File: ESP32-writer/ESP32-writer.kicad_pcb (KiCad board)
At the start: 2 copper layers, 27.2 x 30.6 mm, 17 parts, among them J1 USB2.0_C, J2 UART-OUTPUT, J3 USB2.0_C, Q1 2N7002, Q2 2N7002, U1 CH340C

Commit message: up
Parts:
- added U2: ESP-Prog-ProgramCOM-SEND, $74th:BoxPinHeader_2x03_P1.27mm_Vertical, F.Cu at (93.9, 68.6)
- moved C3 11.9 mm to (80.3, 64.4), turned to 180 degrees
- moved Q2 3.51 mm to (86.2, 86.8)
- moved Q1 3.50 mm to (86.2, 83.3)
- moved J2 2.60 mm to (94.0, 90.2)
- moved R3 2.33 mm to (79.8, 66.9)
- moved C2 1.44 mm to (79.9, 68.8)
- moved R1 1.10 mm to (80.0, 70.7)
- moved R2 0.77 mm to (80.0, 72.7)
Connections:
- Q1 pad 1: RTS -> DTR
- Q1 pad 2: DTS -> RTS
- Q2 pad 1: DTS -> RTS
- Q2 pad 2: RTS -> DTR
- U1 pad 13: DTS -> DTR
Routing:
- net DTS: track 23.1 -> 0.00 mm
- net DTR: track 0.00 -> 23.0 mm
- net RESET: track 10.4 -> 31.1 mm, vias 0 -> 2
- net +5V: track 89.9 -> 103.7 mm
- net BOOT: track 9.45 -> 22.2 mm
- net RXD: track 37.9 -> 48.4 mm
- net Net-(D1-Pad2): track 2.21 -> 7.86 mm, vias 0 -> 2
- net TXD: track 30.8 -> 35.3 mm
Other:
- board size 27.2 x 30.6 mm -> 31.2 x 30.5 mm
- board text added: "ESP32-Writer v2.0.0"
- board text added: "JLCJLCJLCJLC"
- board text removed: "ESP32-Writer v2.0"

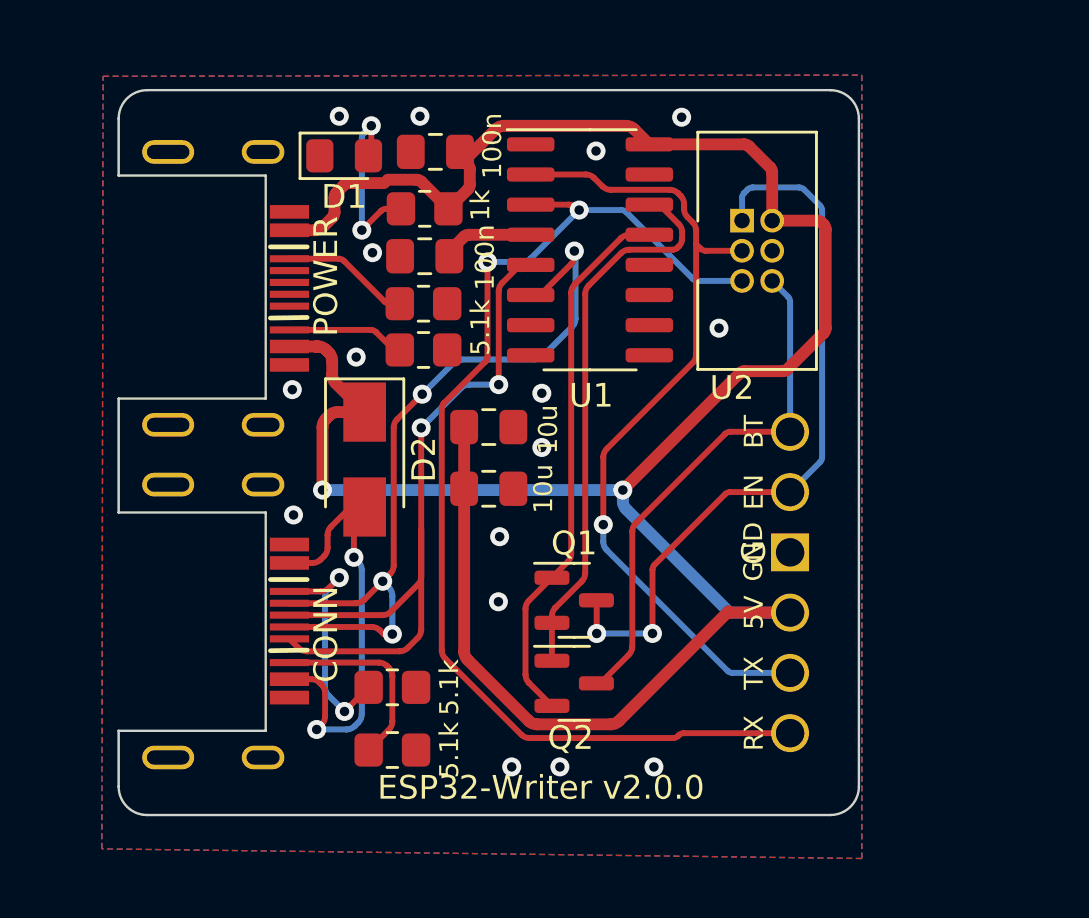
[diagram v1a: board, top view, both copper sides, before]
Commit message: ESP32-C3-WROOM-02
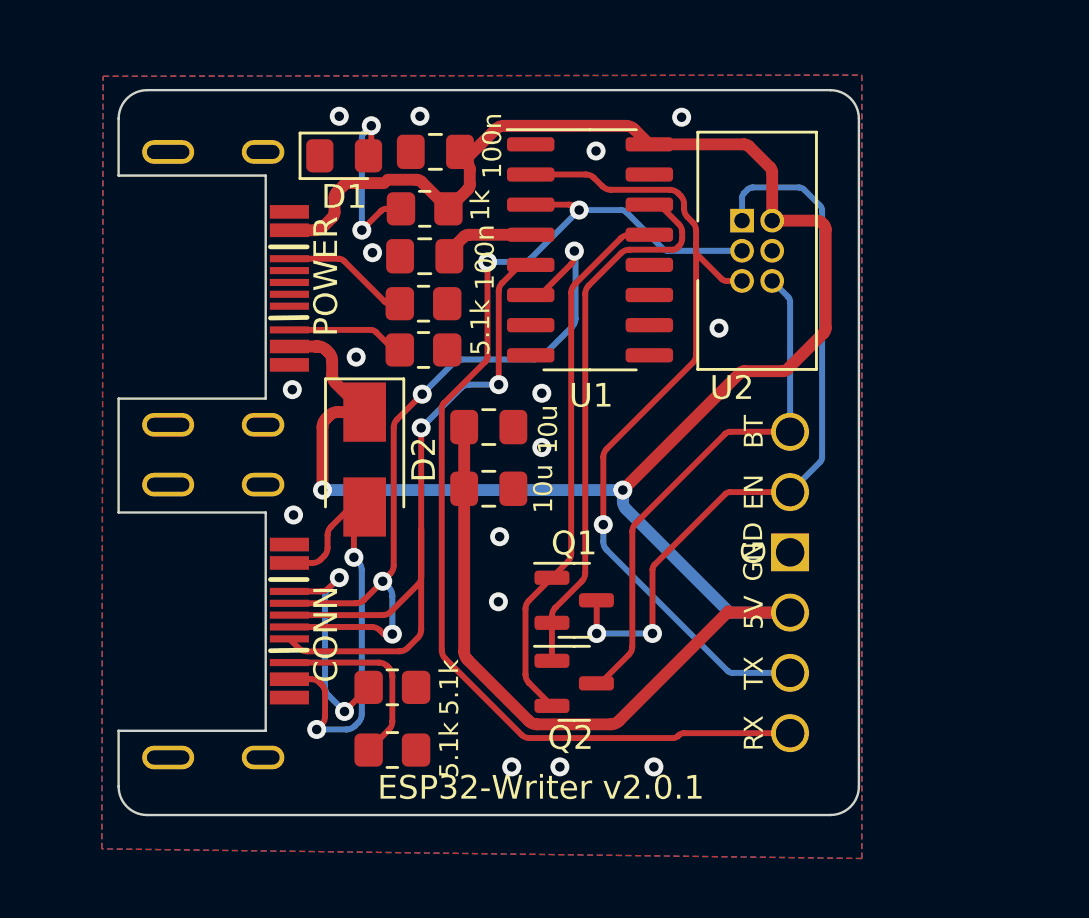
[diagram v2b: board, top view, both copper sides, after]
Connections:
- net +3V3 renamed +3.3V
- U2 pad 3: TXD -> RXD
- U2 pad 5: RXD -> TXD
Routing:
- net RXD: track 48.4 -> 47.9 mm
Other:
- board text added: "ESP32-Writer v2.0.1"
- board text removed: "ESP32-Writer v2.0.0"

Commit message: up
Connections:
- C2 pad 1: +3.3V -> Net-(SW1A-A)
- J1 pad 1: +5V -> Net-(J1-VBUS)
- J3 pad 1: Net-(D2-A) -> Net-(J3-VBUS)
- U1 pad 4: +3.3V -> Net-(SW1A-B)
- U1 pad 7: unconnected-(U1-NC) -> Net-(U1-XI)
- U1 pad 8: unconnected-(U1-OUT) -> Net-(U1-XO)
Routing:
- net Net-(J3-VBUS): track 0.00 -> 19.2 mm, vias 0 -> 2
- net Net-(D2-A): track 19.2 -> 0.00 mm, vias 2 -> 0
- net Net-(SW1A-A): track 0.00 -> 3.90 mm
- net +3.3V: track 3.90 -> 0.00 mm

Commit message: update esp32-writer
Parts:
- removed C2: 100n, $74th:Capacitor_0805_2012
- added C5: 100n, $74th:Capacitor_0805_2012, F.Cu at (82.9, 72.0)
- added C6: 22p, $74th:Capacitor_0805_2012, F.Cu at (91.6, 87.7)
- added C7: 22p, $74th:Capacitor_0805_2012, F.Cu at (83.7, 87.9)
- added C8: 1u, $74th:Capacitor_0805_2012, F.Cu at (91.8, 73.0)
- added F1: Polyfuse, $74th:ResettableFuse_KT6-1100SMDI, F.Cu at (79.1, 85.2)
- added F2: Polyfuse, $74th:ResettableFuse_KT6-1100SMDI, F.Cu at (79.1, 69.1)
- added J4: ESP-Prog-ProgramCOM-SEND, $74th:BoxPinHeader_2x03_P1.27mm_Vertical, F.Cu at (98.4, 67.6)
- added JP1: Jumper_3_Open, Jumper:SolderJumper-3_P1.3mm_Open_RoundedPad1.0x1.5mm_NumberLabels, F.Cu at (83.5, 77.7)
- added JP3: Jumper_2_Open, Jumper:SolderJumper-2_P1.3mm_Open_RoundedPad1.0x1.5mm, F.Cu at (83.4, 83.8)
- added Y1: 12M, $74th:Crystal_SMD_3225-4Pin_3.2x2.5mm_HandSoldering, F.Cu at (87.8, 87.8)
- C1: value 10u -> 1u
- C3: value 100n -> 1u
- C4: value 10u -> 100n
- D1: value LED -> D_Schottky; footprint $74th:LED_0805_2012Metric_Pad1.15x1.40mm_HandSolder -> $74th:D_SMA
- D2: value D_Schottky -> LED; footprint $74th:D_SMA -> $74th:LED_0805_2012Metric_Pad1.15x1.40mm_HandSolder
- J1: footprint $74th:USB-C-12-Pin-MidMount-ali-v4 -> $74th:USB-C-12-Pin-MidMount-ali-v5
- J2: value UART-OUTPUT -> USB2.0_C; footprint esp32-dev-board:UART -> $74th:USB-C-12-Pin-MidMount-ali-v5
- J3: value USB2.0_C -> UART-OUTPUT; footprint $74th:USB-C-12-Pin-MidMount-ali-v4 -> esp32-dev-board:UART
- R1, R2, R4: moved to B.Cu
- R3: value 1k -> 5.1k; moved to B.Cu
- R5: value 5.1k -> 200; moved to B.Cu
- U1: value CH340C -> AMS1117-3.3; footprint Package_SO:SOP-16_3.9x9.9mm_P1.27mm -> Package_TO_SOT_SMD:SOT-223-3_TabPin2
- U2: value ESP-Prog-ProgramCOM-SEND -> CH340G; footprint $74th:BoxPinHeader_2x03_P1.27mm_Vertical -> Package_SO:SOP-16_3.9x9.9mm_P1.27mm
- moved J3 29.8 mm to (102.1, 73.8)
- moved J2 27.7 mm to (67.0, 84.3), turned to -90 degrees
- moved R5 22.1 mm to (82.9, 67.8), turned to 90 degrees
- moved C4 15.6 mm to (96.7, 85.2), turned to 180 degrees
- moved C3 14.2 mm to (93.6, 69.5), turned to 90 degrees
- moved Q2 14.1 mm to (96.6, 77.3)
- moved D1 12.6 mm to (79.0, 76.9), turned to -90 degrees
- moved C1 12.1 mm to (83.0, 63.9), turned to 180 degrees
- moved U2 11.5 mm to (89.9, 79.4)
- moved D2 11.1 mm to (82.9, 67.8), turned to 90 degrees
- moved Q1 10.5 mm to (96.5, 81.3)
- moved R2 10.5 mm to (79.4, 83.1)
- moved J1 7.20 mm to (67.0, 70.1)
- moved R3 4.16 mm to (79.1, 71.0), turned to 0 degrees
- moved U1 2.54 mm to (88.9, 67.0), turned to -90 degrees
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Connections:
- C3 pad 1: +5V -> +3V3
- C4 pad 1: +5V -> RESET
- D1 pad 1: GND -> +5V
- D2 pad 1: +5V -> GND
- J2 pad 1: RXD -> Net-(J2-VBUS)
- J2 pad 2: TXD -> DM
- J2 pad 3: +5V -> DP
- J2 pad 5: RESET -> Net-(J2-CC1)
- J2 pad 6: BOOT -> Net-(J2-CC2)
- J3 pad 1: Net-(J3-VBUS) -> RXD
- J3 pad 2: DM -> TXD
- J3 pad 3: DP -> +5V
- J3 pad 4: GND -> +3V3
- J3 pad 5: Net-(J3-CC1) -> GND
- J3 pad 6: Net-(J3-CC2) -> RESET
- R2 pad 1: Net-(J1-CC2) -> Net-(J2-CC1)
- R3 pad 1: +5V -> Net-(J1-CC2)
- R3 pad 2: Net-(D1-A) -> GND
- R4 pad 1: Net-(J3-CC1) -> Net-(J2-CC2)
- R5 pad 1: Net-(J3-CC2) -> +5V
- R5 pad 2: GND -> Net-(D2-A)
- U1 pad 2: TXD -> +3V3
- U1 pad 3: RXD -> +5V
- U2 pad 1: RESET -> GND
- U2 pad 2: +5V -> TXD
- U2 pad 4: GND -> Net-(JP1-C)
- U2 pad 5: TXD -> DP
- U2 pad 6: BOOT -> DM
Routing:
- net +3V3: track 0.00 -> 54.2 mm, vias 0 -> 2
- net +5V: track 103.7 -> 74.1 mm, vias 2 -> 1
- net Net-(J3-VBUS): track 19.2 -> 0.00 mm, vias 2 -> 0
- net DTR: track 23.0 -> 5.54 mm
- net RXD: track 47.9 -> 30.6 mm, vias 2 -> 1
- net DM: track 33.1 -> 17.5 mm, vias 4 -> 3
- net Net-(JP3-B): track 0.00 -> 14.2 mm
- net RTS: track 23.4 -> 10.4 mm
- net Net-(J2-VBUS): track 0.00 -> 12.9 mm
- net DP: track 32.8 -> 20.1 mm
- net Net-(J1-VBUS): track 0.00 -> 12.5 mm
- net Net-(J3-CC1): track 9.94 -> 0.00 mm, vias 2 -> 0
- net GND: track 0.07 -> 9.50 mm, vias 16 -> 26
- net Net-(J3-CC2): track 8.15 -> 0.00 mm
- net TXD: track 35.6 -> 28.1 mm
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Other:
- board size 31.2 x 30.5 mm -> 36.4 x 30.7 mm
- board text added: "ESP32-Writer v2.1.0"
- board text added: "R232"
- board text removed: "ESP32-Writer v2.0.1"

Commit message: type-b
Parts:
- renumbered C5 to C2, C7 to C3, C8 to C4, C6 to C5, C3 to C6, C4 to C7, F2 to F1, F1 to F2, J4 to J3, J3 to J4, JP3 to JP2, Q2 to Q1, Q1 to Q2, R5 to R1, R4 to R3, R1 to R4, R3 to R5
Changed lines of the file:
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@@
     (property "ki_keywords" "cap capacitor")
     (attr smd)
-    (fp_text reference "C8" (at 2.3 0.2 90) (layer "F.SilkS")
+    (fp_text reference "C4" (at 2.3 0.2 90) (layer "F.SilkS")
         (effects (font (size 0.8 0.8) (thickness 0.12)))
     )
@@
     (property "ki_keywords" "cap capacitor")
     (attr smd)
-    (fp_text reference "C5" (at 0 1.45 90) (layer "F.SilkS")
+    (fp_text reference "C2" (at 0 1.45 90) (layer "F.SilkS")
         (effects (font (size 0.8 0.8) (thickness 0.12)))
     )
@@
     (property "ki_keywords" "cap capacitor")
     (attr smd)
-    (fp_text reference "C4" (at 2.3 0.1 90) (layer "F.SilkS")
+    (fp_text reference "C7" (at 2.3 0.1 90) (layer "F.SilkS")
         (effects (font (size 0.8 0.8) (thickness 0.12)))
     )
@@
     (property "ki_keywords" "N-Channel Switching MOSFET")
     (attr smd)
-    (fp_text reference "Q2" (at -2.2625 0.3 90) (layer "F.SilkS")
+    (fp_text reference "Q1" (at -2.2625 0.3 90) (layer "F.SilkS")
         (effects (font (size 1 1) (thickness 0.15)))
     )
@@
     (property "ki_keywords" "resettable fuse PTC PPTC polyfuse polyswitch")
     (attr smd)
-    (fp_text reference "F2" (at 0.1 0.1 90 unlocked) (layer "F.SilkS")
+    (fp_text reference "F1" (at 0.1 0.1 90 unlocked) (layer "F.SilkS")
         (effects (font (size 0.8 0.8) (thickness 0.12)))
     )
@@
     (property "ki_keywords" "resettable fuse PTC PPTC polyfuse polyswitch")
     (attr smd)
-    (fp_text reference "F1" (at 0.3 0.1 90 unlocked) (layer "F.SilkS")
+    (fp_text reference "F2" (at 0.3 0.1 90 unlocked) (layer "F.SilkS")
         (effects (font (size 0.8 0.8) (thickness 0.12)))
     )
@@
     (property "Sheetname" "")
     (attr through_hole)
-    (fp_text reference "J3" (at 7.62 -5.715 -90 unlocked) (layer "F.Fab")
+    (fp_text reference "J4" (at 7.62 -5.715 -90 unlocked) (layer "F.Fab")
         (effects (font (size 1 1) (thickness 0.15)))
     )
@@
     (property "ki_description" "Jumper, 2-pole, open")
     (property "ki_keywords" "Jumper SPST")
-    (fp_text reference "JP3" (at -0.1 2.3 90) (layer "F.SilkS")
+    (fp_text reference "JP2" (at -0.1 2.3 90) (layer "F.SilkS")
         (effects (font (size 1 1) (thickness 0.15)))
     )
@@
     (property "Sheetname" "")
     (attr through_hole)
-    (fp_text reference "J4" (at 1.435 -3.97 90) (layer "F.SilkS")
+    (fp_text reference "J3" (at 1.435 -3.97 90) (layer "F.SilkS")
         (effects (font (size 1 1) (thickness 0.15)))
     )
@@
     (property "ki_keywords" "cap capacitor")
     (attr smd)
-    (fp_text reference "C7" (at 0.3 -1.4 90) (layer "F.SilkS")
+    (fp_text reference "C3" (at 0.3 -1.4 90) (layer "F.SilkS")
         (effects (font (size 0.8 0.8) (thickness 0.12)))
     )
@@
     (property "ki_keywords" "N-Channel Switching MOSFET")
     (attr smd)
-    (fp_text reference "Q1" (at -2.3 0 90) (layer "F.SilkS")
+    (fp_text reference "Q2" (at -2.3 0 90) (layer "F.SilkS")
         (effects (font (size 1 1) (thickness 0.15)))
     )
@@
     (property "ki_keywords" "cap capacitor")
     (attr smd)
-    (fp_text reference "C3" (at 0 1.5 90) (layer "F.SilkS")
+    (fp_text reference "C6" (at 0 1.5 90) (layer "F.SilkS")
         (effects (font (size 0.8 0.8) (thickness 0.12)))
     )
@@
     (property "ki_keywords" "cap capacitor")
     (attr smd)
-    (fp_text reference "C6" (at 0 -1.7 90) (layer "F.SilkS")
+    (fp_text reference "C5" (at 0 -1.7 90) (layer "F.SilkS")
         (effects (font (size 0.8 0.8) (thickness 0.12)))
     )
@@
     (property "ki_keywords" "R res resistor")
     (attr smd)
-    (fp_text reference "R4" (at 2.4 0.1 90) (layer "B.SilkS")
+    (fp_text reference "R3" (at 2.4 0.1 90) (layer "B.SilkS")
         (effects (font (size 0.8 0.8) (thickness 0.12)) (justify mirror))
     )
@@
     (property "ki_keywords" "R res resistor")
     (attr smd)
-    (fp_text reference "R1" (at 0.1 -1.7 90) (layer "B.SilkS")
+    (fp_text reference "R4" (at 0.1 -1.7 90) (layer "B.SilkS")
         (effects (font (size 0.8 0.8) (thickness 0.12)) (justify mirror))
     )
@@
     (property "ki_keywords" "R res resistor")
     (attr smd)
-    (fp_text reference "R5" (at 0 -1.5 90) (layer "B.SilkS")
+    (fp_text reference "R1" (at 0 -1.5 90) (layer "B.SilkS")
         (effects (font (size 0.8 0.8) (thickness 0.12)) (justify mirror))
     )
@@
     (property "ki_keywords" "R res resistor")
     (attr smd)
-    (fp_text reference "R3" (at 2.4 -0.1 90) (layer "B.SilkS")
+    (fp_text reference "R5" (at 2.4 -0.1 90) (layer "B.SilkS")
         (effects (font (size 0.8 0.8) (thickness 0.12)) (justify mirror))
     )

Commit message: type ch340g
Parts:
- removed the C3 at (83.7, 87.9)
- removed the C4 at (91.8, 73.0)
- removed C5: 22p, $74th:Capacitor_0805_2012
- removed F1, F2: Polyfuse, $74th:ResettableFuse_KT6-1100SMDI
- removed the J3 at (98.4, 67.6)
- removed JP1: Jumper_3_Open, Jumper:SolderJumper-3_P1.3mm_Open_RoundedPad1.0x1.5mm_NumberLabels
- removed JP2: Jumper_2_Open, Jumper:SolderJumper-2_P1.3mm_Open_RoundedPad1.0x1.5mm
- removed Y1: 12M, $74th:Crystal_SMD_3225-4Pin_3.2x2.5mm_HandSoldering
- C1: value 1u -> 10u
- C3: renamed from C6; value 1u -> 100n
- C4: renamed from C7; value 100n -> 10u
- D1: value D_Schottky -> LED; footprint $74th:D_SMA -> $74th:LED_0805_2012Metric_Pad1.15x1.40mm_HandSolder
- D2: value LED -> D_Schottky; footprint $74th:LED_0805_2012Metric_Pad1.15x1.40mm_HandSolder -> $74th:D_SMA
- J1: footprint $74th:USB-C-12-Pin-MidMount-ali-v5 -> $74th:USB-C-12-Pin-MidMount-ali-v4
- J2: value USB2.0_C -> UART-OUTPUT; footprint $74th:USB-C-12-Pin-MidMount-ali-v5 -> esp32-dev-board:UART
- J3: renamed from J4; value UART-OUTPUT -> USB2.0_C; footprint esp32-dev-board:UART -> $74th:USB-C-12-Pin-MidMount-ali-v4
- R1: renamed from R4; moved to F.Cu
- R2: moved to F.Cu
- R3: renamed from R5; value 5.1k -> 1k; moved to F.Cu
- R4: renamed from R3; moved to F.Cu
- R5: renamed from R1; value 200 -> 5.1k; moved to F.Cu
- U1: value AMS1117-3.3 -> CH340C; footprint Package_TO_SOT_SMD:SOT-223-3_TabPin2 -> Package_SO:SOP-16_3.9x9.9mm_P1.27mm
- U2: value CH340G -> ESP-Prog-ProgramCOM-SEND; footprint Package_SO:SOP-16_3.9x9.9mm_P1.27mm -> $74th:BoxPinHeader_2x03_P1.27mm_Vertical
- moved J3 29.8 mm to (74.2, 84.2)
- moved J2 27.7 mm to (94.0, 90.2), turned to 90 degrees
- moved R5 22.1 mm to (78.6, 89.5), turned to 0 degrees
- moved C4 15.6 mm to (82.6, 78.6), turned to 0 degrees
- moved C3 14.2 mm to (80.3, 64.4), turned to 180 degrees
- moved Q2 14.1 mm to (86.2, 86.8)
- moved D1 12.6 mm to (76.5, 64.6), turned to 0 degrees
- moved C1 12.1 mm to (82.6, 76.0), turned to 0 degrees
- moved U2 11.5 mm to (93.9, 68.6)
- moved D2 11.1 mm to (77.4, 77.4), turned to -90 degrees
- moved Q1 10.5 mm to (86.2, 83.3)
- moved R2 10.5 mm to (80.0, 72.7)
- moved J1 7.20 mm to (74.2, 70.2)
- moved C2 4.39 mm to (79.9, 68.8), turned to 180 degrees
- moved R3 4.16 mm to (79.8, 66.9), turned to 180 degrees
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- renumbered Q2 to Q1, Q1 to Q2
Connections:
- C2 pad 1: Net-(JP1-B) -> +3.3V
- C3 pad 1: +3V3 -> +5V
- C4 pad 1: RESET -> +5V
- D1 pad 1: +5V -> GND
- D2 pad 1: GND -> +5V
- J1 pad 1: Net-(J1-VBUS) -> +5V
- J2 pad 1: Net-(J2-VBUS) -> RXD
- J2 pad 2: DM -> TXD
- J2 pad 3: DP -> +5V
- J2 pad 5: Net-(J2-CC1) -> RESET
- J2 pad 6: Net-(J2-CC2) -> BOOT
- J3 pad 1: RXD -> Net-(D2-A)
- J3 pad 2: TXD -> DM
- J3 pad 3: +5V -> DP
- J3 pad 4: +3V3 -> GND
- J3 pad 5: GND -> Net-(J3-CC1)
- J3 pad 6: RESET -> Net-(J3-CC2)
- R2 pad 1: Net-(J2-CC1) -> Net-(J1-CC2)
- R3 pad 1: Net-(J1-CC2) -> +5V
- R3 pad 2: GND -> Net-(D1-A)
- R4 pad 1: Net-(J2-CC2) -> Net-(J3-CC1)
- R5 pad 1: +5V -> Net-(J3-CC2)
- R5 pad 2: Net-(D2-A) -> GND
- U1 pad 2: +3V3 -> TXD
- U1 pad 3: +5V -> RXD
- U2 pad 1: GND -> RESET
- U2 pad 2: TXD -> +5V
- U2 pad 4: Net-(JP1-C) -> GND
- U2 pad 5: DP -> TXD
- U2 pad 6: DM -> BOOT
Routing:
- net +3V3: track 54.2 -> 0.00 mm, vias 2 -> 0
- net +5V: track 74.1 -> 103.7 mm, vias 1 -> 2
- net DTR: track 5.54 -> 23.0 mm
- net RXD: track 30.6 -> 47.9 mm, vias 1 -> 2
- net Net-(D2-A): track 2.96 -> 19.2 mm, vias 1 -> 2
- net DM: track 17.5 -> 33.1 mm, vias 3 -> 4
- net Net-(JP3-B): track 14.2 -> 0.00 mm
- net RTS: track 10.4 -> 23.4 mm
- net Net-(J2-VBUS): track 12.9 -> 0.00 mm
- net DP: track 20.1 -> 32.8 mm
- net Net-(J1-VBUS): track 12.5 -> 0.00 mm
- net Net-(J3-CC1): track 0.00 -> 9.94 mm, vias 0 -> 2
- net GND: track 9.50 -> 0.07 mm, vias 26 -> 16
- net Net-(J3-CC2): track 0.00 -> 8.15 mm
- net TXD: track 28.1 -> 35.6 mm
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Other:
- board size 36.4 x 30.7 mm -> 31.2 x 30.5 mm
- board text added: "ESP32-Writer v2.0.1"
- board text removed: "ESP32-Writer v2.1.0"
- board text removed: "R232"
